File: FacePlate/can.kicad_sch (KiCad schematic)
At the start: 23 parts, among them U5 MCP2515-xST, U6 SN65HVD233, Y2 ABM3-8.000MHZ-D2Y-T

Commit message: faceplate. broken.
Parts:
- U5: footprint Package_SO:TSSOP-20_4.4x6.5mm_P0.65mm -> bots:TSSOP-20_4.4x6.5mm_P0.65mm; symbol Interface_CAN_LIN:MCP2515-xST -> bots:MCP2515T-I/ST; JLC (none) -> TSSOP-20; JLC Extended (none) -> yes; LCSC C15193 -> C185941; MPN (none) -> MCP2515T-I/ST; Manufacturer (none) -> Microchip; Price (none) -> 1.2541
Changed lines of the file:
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@@
 	)
 	(symbol
-		(lib_id "Interface_CAN_LIN:MCP2515-xST")
+		(lib_id "bots:MCP2515T-I/ST")
 		(at 158.75 78.74 0)
 		(mirror y)
@@
 			)
 		)
-		(property "Footprint" "Package_SO:TSSOP-20_4.4x6.5mm_P0.65mm"
+		(property "Footprint" "bots:TSSOP-20_4.4x6.5mm_P0.65mm"
 			(at 158.75 101.6 0)
 			(effects
@@
 			)
 		)
-		(property "Description" ""
+		(property "Description" "Stand-Alone CAN Controller with SPI Interface, TSSOP-20"
 			(at 158.75 78.74 0)
 			(effects
@@
 					(size 1.27 1.27)
 				)
+				(hide yes)
 			)
 		)
-		(property "LCSC" "C15193"
+		(property "LCSC" "C185941"
 			(at 158.75 78.74 0)
 			(effects
+				(font
+					(size 1.27 1.27)
+				)
+				(hide yes)
+			)
+		)
+		(property "MPN" "MCP2515T-I/ST"
+			(at 158.75 78.74 0)
+			(effects
+				(font
+					(size 1.27 1.27)
+				)
+				(hide yes)
+			)
+		)
+		(property "Manufacturer" "Microchip"
+			(at 158.75 78.74 0)
+			(effects
+				(font
+					(size 1.27 1.27)
+				)
+				(hide yes)
+			)
+		)
+		(property "Price" "1.2541"
+			(at 158.75 78.74 0)
+			(effects
+				(font
+					(size 1.27 1.27)
+				)
+				(hide yes)
+			)
+		)
+		(property "JLC" "TSSOP-20"
+			(at 158.75 78.74 0)
+			(effects
+				(font
+					(size 1.27 1.27)
+				)
+				(hide yes)
+			)
+		)
+		(property "JLC Extended" "yes"
+			(at 158.75 78.74 0)
+			(effects

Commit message: faceplate global files working
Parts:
- R10, R11, R12, R13, R14, R15, R16, R17, R18: symbol bots:0R -> bots:R_0R; JLC (none) -> 0603; JLC Extended (none) -> no; MPN (none) -> 0603WAF0000T5E; Manufacturer (none) -> UNI-ROYAL(Uniroyal Elec); Price (none) -> 0.001
- R2, R3, R36: footprint Resistor_SMD:R_0603_1608Metric -> bots:R_0603_1608Metric; symbol Device:R -> bots:R_10k; JLC (none) -> 0603; JLC Extended (none) -> no; MPN (none) -> 0603WAF1002T5E; Manufacturer (none) -> UNI-ROYAL(Uniroyal Elec); Price (none) -> 0.0008
- Y2: footprint footprints:XTAL_ABM3-8.000MHZ-D2Y-T_ABR -> bots:ABM3
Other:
- moved on the sheet: R10, R11, R12, R13, R18

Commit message: added a title block
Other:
- company: (none) -> The Bots
- title: (none) -> Faceplate
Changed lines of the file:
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@@
 	(generator_version "9.0")
 	(paper "A4")
+	(title_block
+		(title "Faceplate")
+		(date "2024-02-04")
+		(rev "V1.0")
+		(company "The Bots")
+	)
 	(text "CAN Transmitter\n"
 		(exclude_from_sim no)

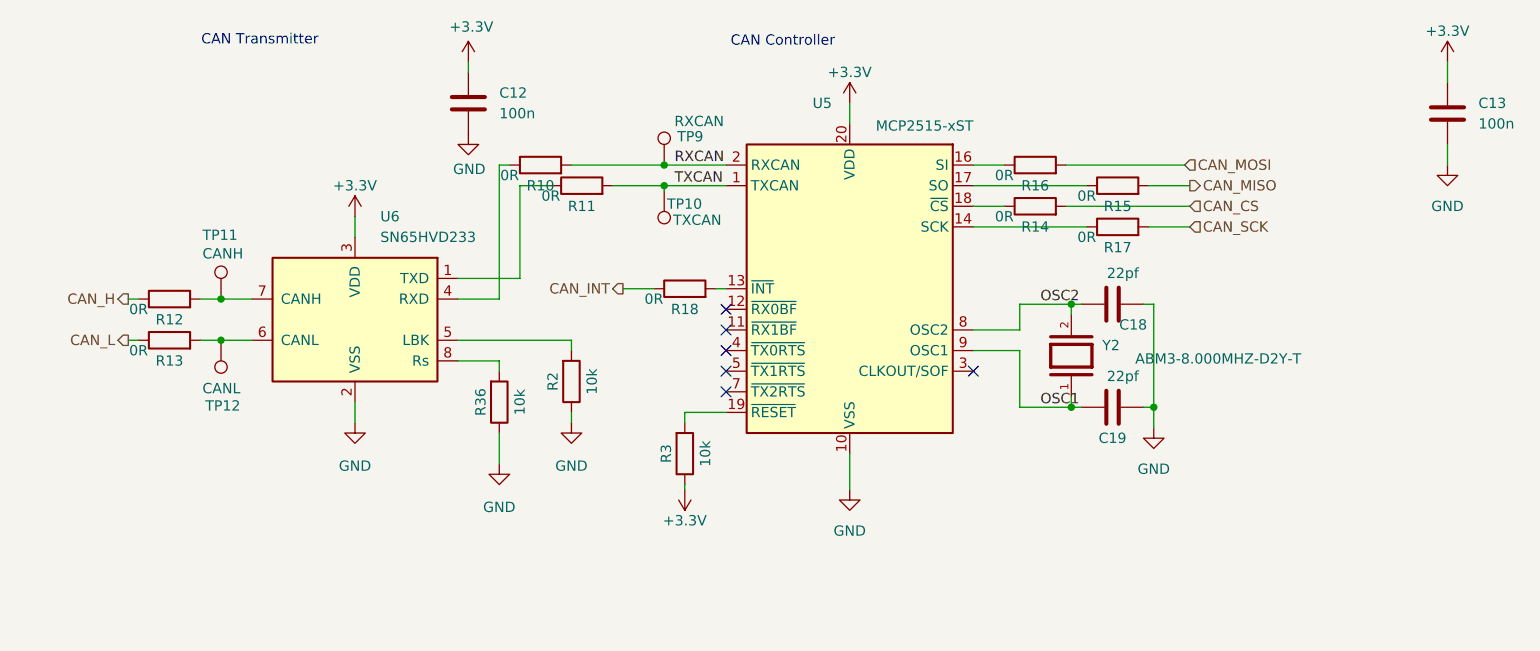
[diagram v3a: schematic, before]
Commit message: wip faceplate 2.0 schematic
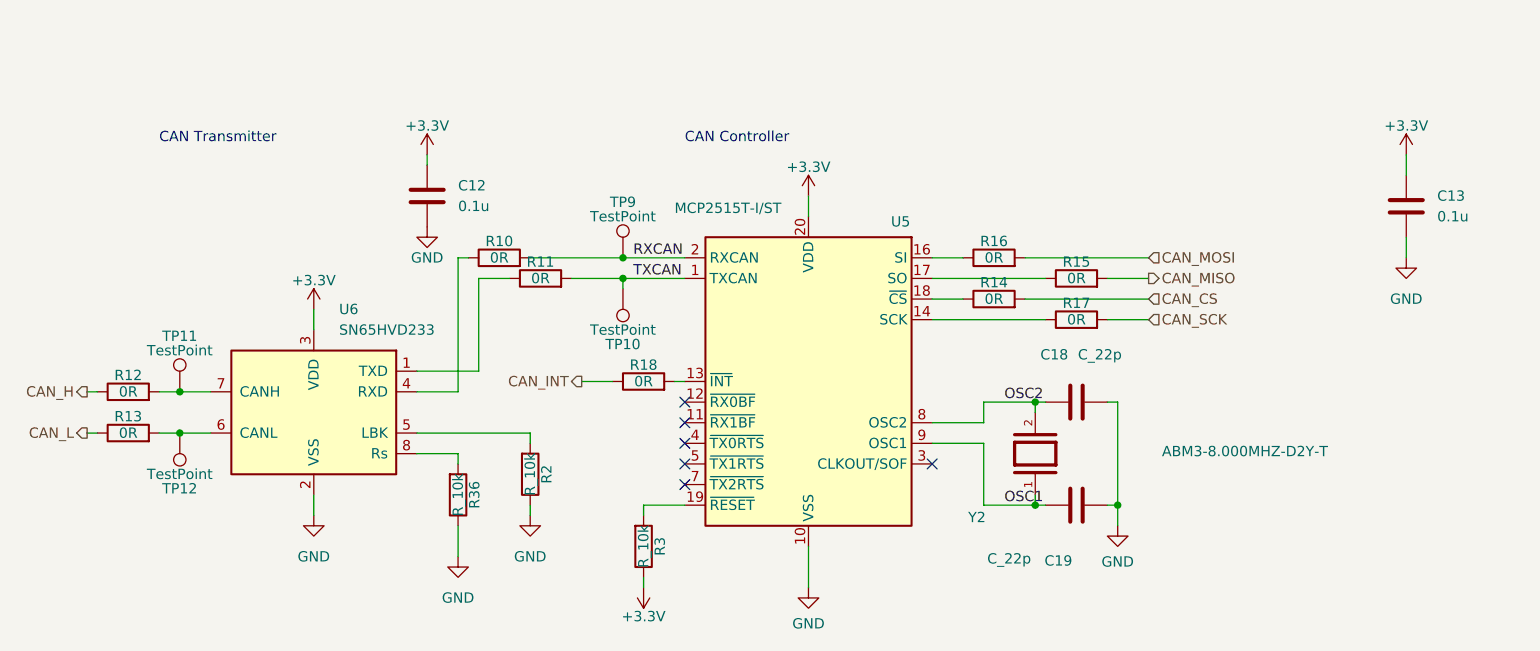
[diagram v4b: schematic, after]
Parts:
- C12, C13: value 100n -> 0.1u; footprint bots:C_0402_1005Metric -> bots:C_0603_1608Metric; JLC (none) -> 0603; JLC Extended (none) -> no; LCSC C307331 -> C14663; MPN (none) -> CC0603KRX7R9BB104; Manufacturer (none) -> YAGEO; Price (none) -> 0.0021
- C18, C19: value 22pf -> C_22p; footprint Capacitor_SMD:C_0603_1608Metric -> bots:C_0603_1608Metric
- R2, R3, R36: value 10k -> R_10k
- TP10: value TXCAN -> TestPoint; footprint TestPoint:TestPoint_Pad_D1.0mm -> (none)
- TP11: value CANH -> TestPoint; footprint TestPoint:TestPoint_Pad_D1.0mm -> (none)
- TP12: value CANL -> TestPoint; footprint TestPoint:TestPoint_Pad_D1.0mm -> (none)
- TP9: value RXCAN -> TestPoint; footprint TestPoint:TestPoint_Pad_D1.0mm -> (none)
- U5: value MCP2515-xST -> MCP2515T-I/ST
- Y2: MANUFACTURER Cardinal Components -> (none)
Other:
- moved on the sheet: C12, C13, C18, C19, R10, R11, R12, R13, R14, R15, R16, R17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

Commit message: fix models
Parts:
- renumbered C13 to C10, C12 to C7, C18 to C8, C19 to C9, R12 to R11, R13 to R12, R36 to R13, R10 to R14, R2 to R15, R11 to R16, R18 to R17, R3 to R18, R16 to R19, R14 to R20, R15 to R21, R17 to R22, TP11 to TP1, TP12 to TP2, TP9 to TP3, TP10 to TP4, U6 to U4, Y2 to Y1

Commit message: old-annotated schematic
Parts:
- renumbered C10 to C13, C8 to C18, C9 to C19, R13 to R, R14 to R10, R16 to R11, R11 to R12, R12 to R13, R20 to R14, R21 to R15, R19 to R16, R22 to R17, R17 to R18, R15 to R2, R18 to R3, U4 to U6, Y1 to Y2
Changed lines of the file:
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@@
 		(in_pos_files yes)
 		(dnp no)
-		(property "Reference" "R22"
+		(property "Reference" "R17"
 			(at 186.69 80.518 90)
 			(show_name no)
@@
 			(project "FacePlate"
 				(path "/e63e39d7-6ac0-4ffd-8aa3-1841a4541b55/99bd3b0c-5cef-43ec-97f5-6b19c715565b"
-					(reference "R22")
+					(reference "R17")
 					(unit 1)
 				)
@@
 		(in_pos_files yes)
 		(dnp no)
-		(property "Reference" "C9"
-			(at 186.182 112.268 90)
+		(property "Reference" "C19"
+			(at 187.452 109.982 90)
 			(show_name no)
 			(do_not_autoplace no)
@@
 		)
 		(property "Value" "C_22p"
-			(at 181.102 112.014 90)
+			(at 184.658 108.458 90)
 			(show_name no)
 			(do_not_autoplace no)
@@
 			(project "FacePlate"
 				(path "/e63e39d7-6ac0-4ffd-8aa3-1841a4541b55/99bd3b0c-5cef-43ec-97f5-6b19c715565b"
-					(reference "C9")
+					(reference "C19")
 					(unit 1)
 				)
@@
 		(in_pos_files yes)
 		(dnp no)
-		(property "Reference" "R19"
+		(property "Reference" "R16"
 			(at 176.53 72.898 90)
 			(show_name no)
@@
 			(project "FacePlate"
 				(path "/e63e39d7-6ac0-4ffd-8aa3-1841a4541b55/99bd3b0c-5cef-43ec-97f5-6b19c715565b"
-					(reference "R19")
+					(reference "R16")
 					(unit 1)
 				)
@@
 		(in_pos_files yes)
 		(dnp no)
-		(property "Reference" "R12"
+		(property "Reference" "R13"
 			(at 69.85 94.488 90)
 			(show_name no)
@@
 			(project "FacePlate"
 				(path "/e63e39d7-6ac0-4ffd-8aa3-1841a4541b55/99bd3b0c-5cef-43ec-97f5-6b19c715565b"
-					(reference "R12")
+					(reference "R13")
 					(unit 1)
 				)
@@
 		(in_pos_files yes)
 		(dnp no)
-		(property "Reference" "R18"
+		(property "Reference" "R3"
 			(at 135.382 110.49 90)
 			(show_name no)
@@
 			(project "FacePlate"
 				(path "/e63e39d7-6ac0-4ffd-8aa3-1841a4541b55/99bd3b0c-5cef-43ec-97f5-6b19c715565b"
-					(reference "R18")
+					(reference "R3")
 					(unit 1)
 				)
@@
 		(dnp no)
 		(fields_autoplaced yes)
-		(property "Reference" "U4"
+		(property "Reference" "U6"
 			(at 95.8281 81.28 0)
 			(show_name no)
@@
 			(project "FacePlate"
 				(path "/e63e39d7-6ac0-4ffd-8aa3-1841a4541b55/99bd3b0c-5cef-43ec-97f5-6b19c715565b"
-					(reference "U4")
+					(reference "U6")
 					(unit 1)
 				)
@@
 		(in_pos_files yes)
 		(dnp no)
-		(property "Reference" "C8"
-			(at 185.674 86.868 90)
+		(property "Reference" "C18"
+			(at 186.944 87.122 90)
 			(show_name no)
 			(do_not_autoplace no)
@@
 		)
 		(property "Value" "C_22p"
-			(at 192.278 86.868 90)
+			(at 191.77 88.9 90)
 			(show_name no)
 			(do_not_autoplace no)
@@
 			(project "FacePlate"
 				(path "/e63e39d7-6ac0-4ffd-8aa3-1841a4541b55/99bd3b0c-5cef-43ec-97f5-6b19c715565b"
-					(reference "C8")
+					(reference "C18")
 					(unit 1)
 				)
@@
 		(in_pos_files yes)
 		(dnp no)
-		(property "Reference" "R16"
+		(property "Reference" "R11"
 			(at 120.65 75.438 90)
 			(show_name no)
@@
 			(project "FacePlate"
 				(path "/e63e39d7-6ac0-4ffd-8aa3-1841a4541b55/99bd3b0c-5cef-43ec-97f5-6b19c715565b"
-					(reference "R16")
+					(reference "R11")
 					(unit 1)
 				)
@@
 		(dnp no)
 		(fields_autoplaced yes)
-		(property "Reference" "C10"
+		(property "Reference" "C13"
 			(at 231.14 67.3099 0)
 			(show_name no)
@@
 			(project "FacePlate"
 				(path "/e63e39d7-6ac0-4ffd-8aa3-1841a4541b55/99bd3b0c-5cef-43ec-97f5-6b19c715565b"
-					(reference "C10")
+					(reference "C13")
 					(unit 1)
 				)
@@
 		(in_pos_files yes)
 		(dnp no)
-		(property "Reference" "R13"
+		(property "Reference" "R"
 			(at 112.522 104.14 90)
 			(show_name no)
@@
 			(project "FacePlate"
 				(path "/e63e39d7-6ac0-4ffd-8aa3-1841a4541b55/99bd3b0c-5cef-43ec-97f5-6b19c715565b"
-					(reference "R13")
+					(reference "R")
 					(unit 1)
 				)
@@
 		(in_pos_files yes)
 		(dnp no)
-		(property "Reference" "R14"
+		(property "Reference" "R10"
 			(at 115.57 72.898 90)
 			(show_name no)
@@
 			(project "FacePlate"
 				(path "/e63e39d7-6ac0-4ffd-8aa3-1841a4541b55/99bd3b0c-5cef-43ec-97f5-6b19c715565b"
-					(reference "R14")
+					(reference "R10")
 					(unit 1)
 				)
@@
 		(in_pos_files yes)
 		(dnp no)
-		(property "Reference" "R15"
+		(property "Reference" "R2"
 			(at 121.412 101.6 90)
 			(show_name no)
@@
 			(project "FacePlate"
 				(path "/e63e39d7-6ac0-4ffd-8aa3-1841a4541b55/99bd3b0c-5cef-43ec-97f5-6b19c715565b"
-					(reference "R15")
+					(reference "R2")
 					(unit 1)
 				)
@@
 		(in_pos_files yes)
 		(dnp no)
-		(property "Reference" "Y1"
-			(at 175.514 106.172 90)
+		(property "Reference" "Y2"
+			(at 187.198 97.79 90)
 			(show_name no)
 			(do_not_autoplace no)
@@
 			(project "FacePlate"
 				(path "/e63e39d7-6ac0-4ffd-8aa3-1841a4541b55/99bd3b0c-5cef-43ec-97f5-6b19c715565b"
-					(reference "Y1")
+					(reference "Y2")
 					(unit 1)
 				)
@@
 		(in_pos_files yes)
 		(dnp no)
-		(property "Reference" "R21"
+		(property "Reference" "R15"
 			(at 186.69 75.438 90)
 			(show_name no)
@@
 			(project "FacePlate"
 				(path "/e63e39d7-6ac0-4ffd-8aa3-1841a4541b55/99bd3b0c-5cef-43ec-97f5-6b19c715565b"
-					(reference "R21")
+					(reference "R15")
 					(unit 1)
 				)
@@
 		(in_pos_files yes)
 		(dnp no)
-		(property "Reference" "R17"
+		(property "Reference" "R18"
 			(at 133.35 88.138 90)
 			(show_name no)
@@
 			(project "FacePlate"
 				(path "/e63e39d7-6ac0-4ffd-8aa3-1841a4541b55/99bd3b0c-5cef-43ec-97f5-6b19c715565b"
-					(reference "R17")
+					(reference "R18")
 					(unit 1)
 				)
@@
 		(in_pos_files yes)
 		(dnp no)
-		(property "Reference" "R11"
+		(property "Reference" "R12"
 			(at 69.85 89.408 90)
 			(show_name no)
@@
 			(project "FacePlate"
 				(path "/e63e39d7-6ac0-4ffd-8aa3-1841a4541b55/99bd3b0c-5cef-43ec-97f5-6b19c715565b"
-					(reference "R11")
+					(reference "R12")
 					(unit 1)
 				)
@@
 		(in_pos_files yes)
 		(dnp no)
-		(property "Reference" "R20"
+		(property "Reference" "R14"
 			(at 176.53 77.978 90)
 			(show_name no)
@@
 			(project "FacePlate"
 				(path "/e63e39d7-6ac0-4ffd-8aa3-1841a4541b55/99bd3b0c-5cef-43ec-97f5-6b19c715565b"
-					(reference "R20")
+					(reference "R14")
 					(unit 1)
 				)

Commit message: pcb updates
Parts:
- renumbered R to R1
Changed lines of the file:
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@@
 		(in_pos_files yes)
 		(dnp no)
-		(property "Reference" "R"
+		(property "Reference" "R1"
 			(at 112.522 104.14 90)
 			(show_name no)
@@
 			(project "FacePlate"
 				(path "/e63e39d7-6ac0-4ffd-8aa3-1841a4541b55/99bd3b0c-5cef-43ec-97f5-6b19c715565b"
-					(reference "R")
+					(reference "R1")
 					(unit 1)
 				)

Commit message: ch;anges
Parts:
- removed TP1, TP2, TP3, TP4: TestPoint, symbol Connector:TestPoint
- added TP10: TXCAN, TestPoint:TestPoint_Pad_D1.0mm, symbol Connector:TestPoint
- added TP12: CANL, TestPoint:TestPoint_Pad_D1.0mm, symbol Connector:TestPoint
- added TP13: CANH, TestPoint:TestPoint_Pad_D1.0mm, symbol Connector:TestPoint
- added TP9: RXCAN, TestPoint:TestPoint_Pad_D1.0mm, symbol Connector:TestPoint
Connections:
- net RXCAN: now also TP9.1
- net TXCAN: now also TP10.1
- net at R13.2, U6.6 (CANL): now also TP12.1
- net at R12.2, U6.7 (CANH): now also TP13.1
